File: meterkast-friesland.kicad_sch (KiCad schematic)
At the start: 11 parts, among them SW1 63A, SW10 SW_SPDT, SW11 SW_SPDT, SW2 40A / 0,03A, SW3 16A, SW4 25A / 0,03A, SW5 16A, SW6 16A, SW7 16A, SW8 20A, SW9 20A

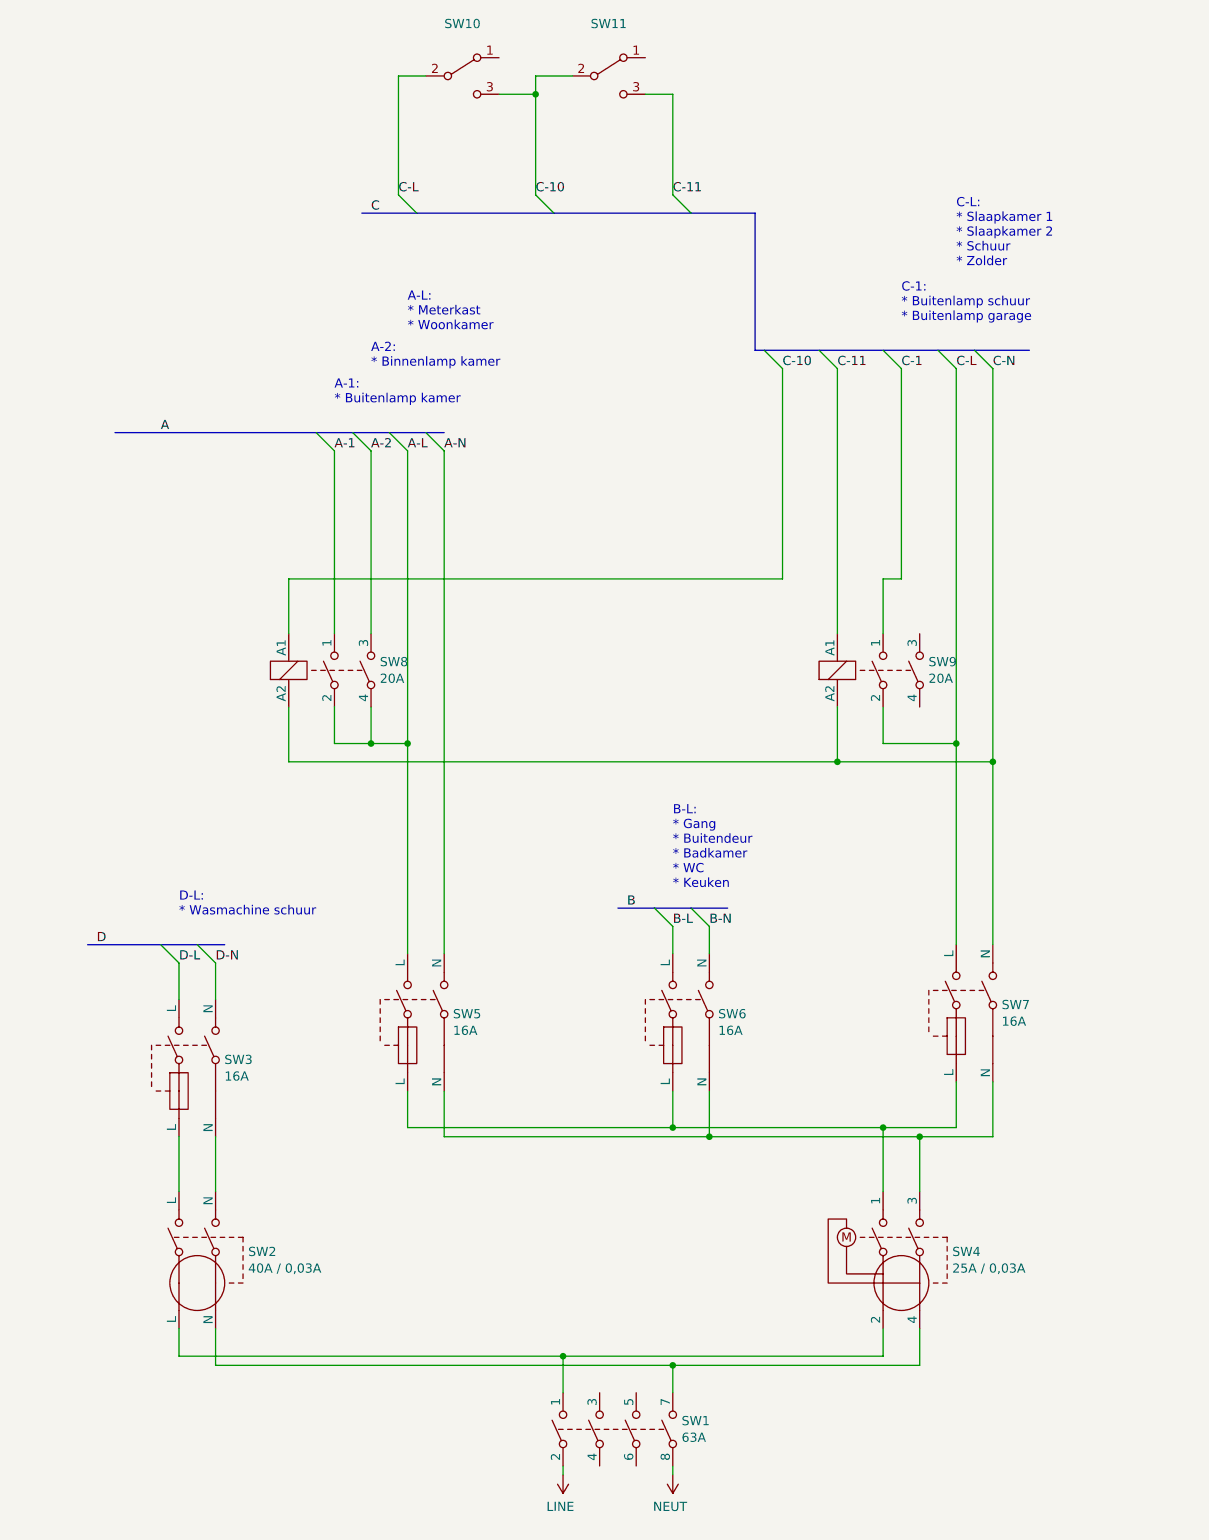
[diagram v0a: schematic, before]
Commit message: Added SW3 (Kookplaat)
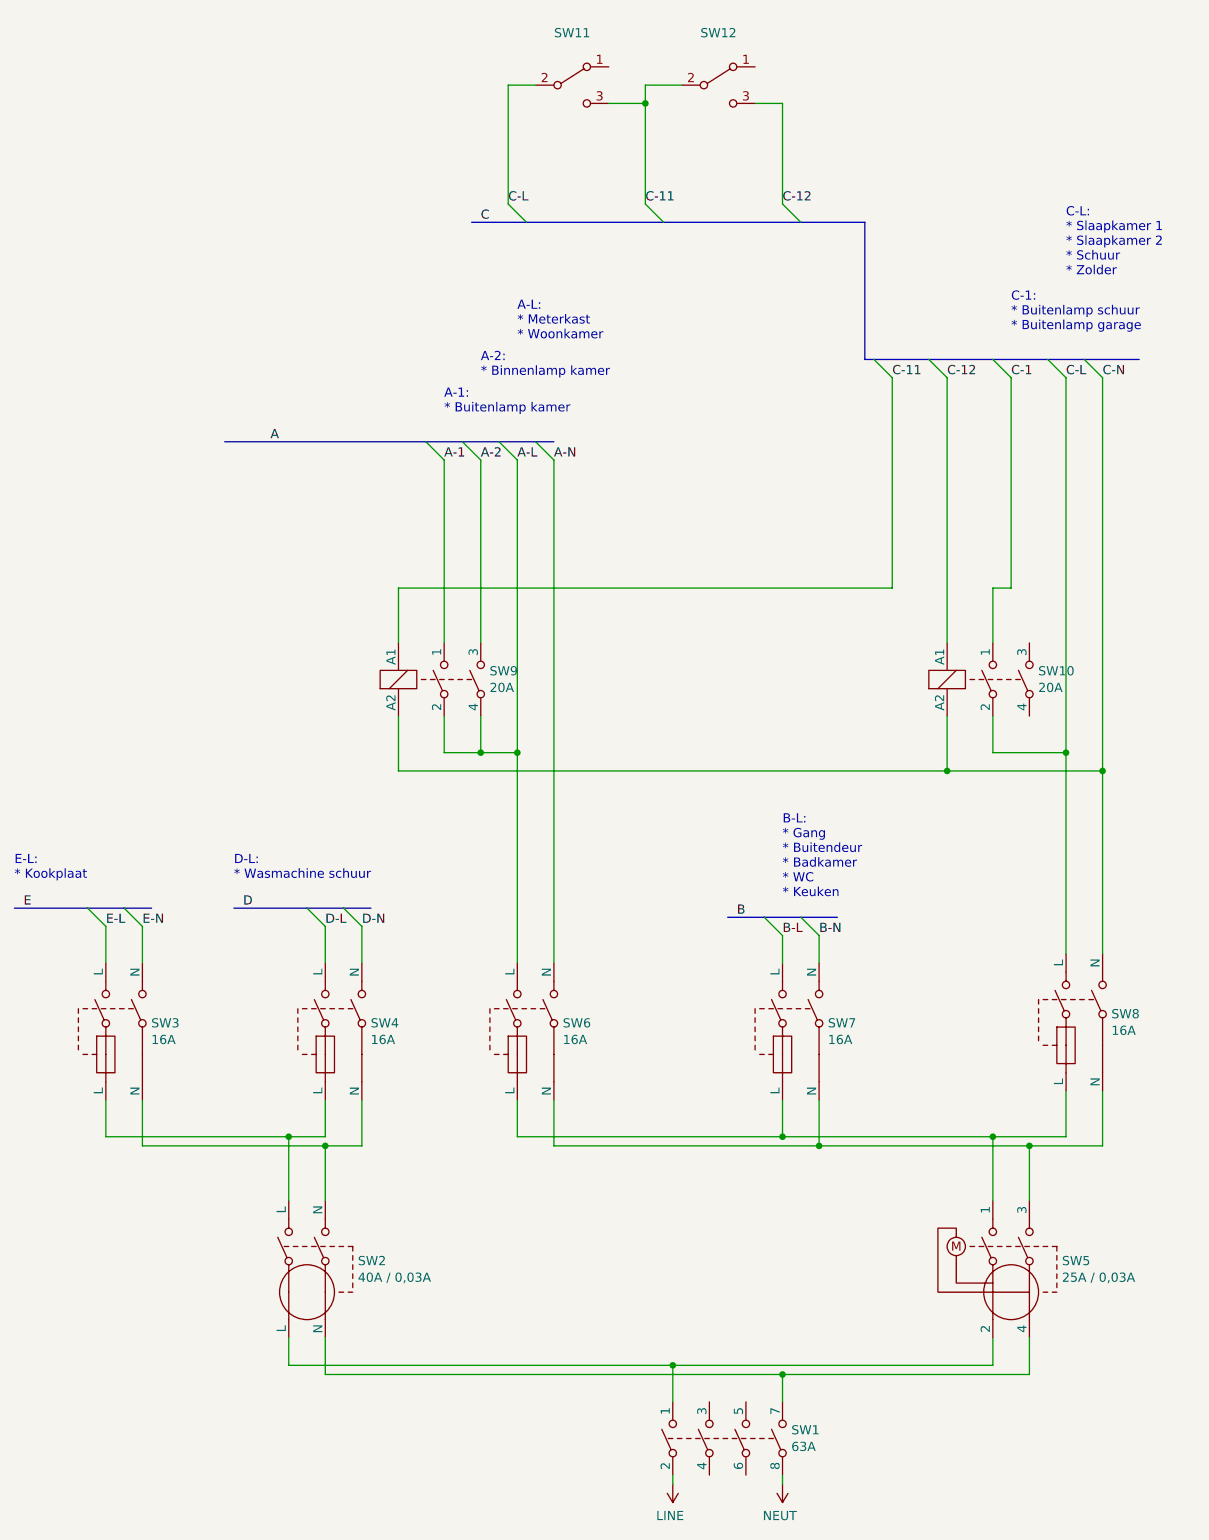
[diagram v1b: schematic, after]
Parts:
- added SW4: 16A, symbol Fuse_Box:CB_2P
- renumbered SW9 to SW10, SW10 to SW11, SW11 to SW12, SW4 to SW5, SW5 to SW6, SW6 to SW7, SW7 to SW8, SW8 to SW9
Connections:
- net C-10 is gone; now on net C-11: SW11.3 (C), SW12.2 (B), SW9.5 (A1)
- net C-11: no longer SW10.5 (A1), SW12.3 (C)
- net D-L: now also SW4.2 (L); no longer SW3.2 (L)
- net D-N: now also SW4.4 (N); no longer SW3.4 (N)
- net at SW2.2 (L), SW3.1 (L): now also SW4.1 (L)
- net at SW2.4 (N), SW3.3 (N): now also SW4.3 (N)
- new net C-12: SW10.5 (A1), SW12.3 (C)
- new net E-L: SW3.2 (L)
- new net E-N: SW3.4 (N)
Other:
- note added: "E-L: * Kookplaat"
- moved on the sheet: SW1, SW10, SW11, SW12, SW2, SW3, SW5, SW6, SW7, SW8, SW9
